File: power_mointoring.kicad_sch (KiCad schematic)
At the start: 30 parts, among them J10 Servo pwr, J11 Vin, J13 VCC, J14 +5V, J7 VCC, J8 Servo pwr, J9 BATT in, SW5 POWER, U3 3V3 REG, U4 DS2438Z+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

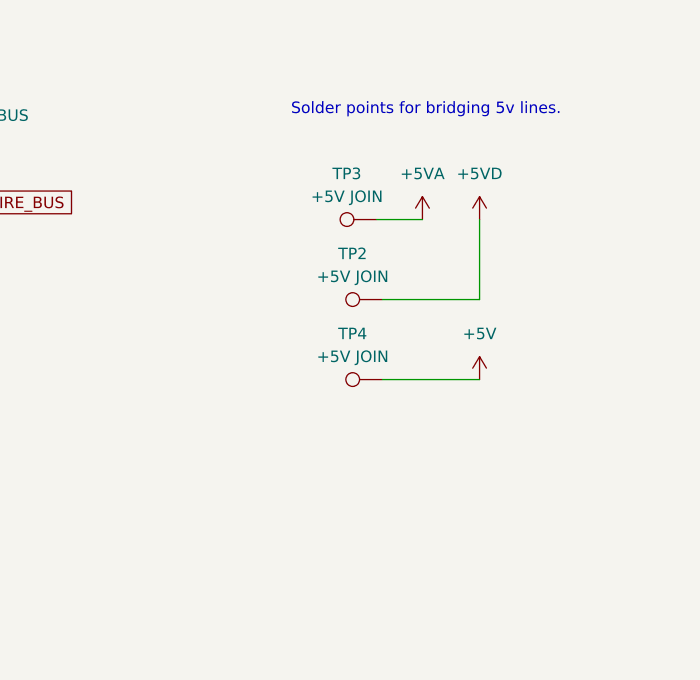
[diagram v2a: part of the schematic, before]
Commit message: Added missing power bridge point for 1 rail.
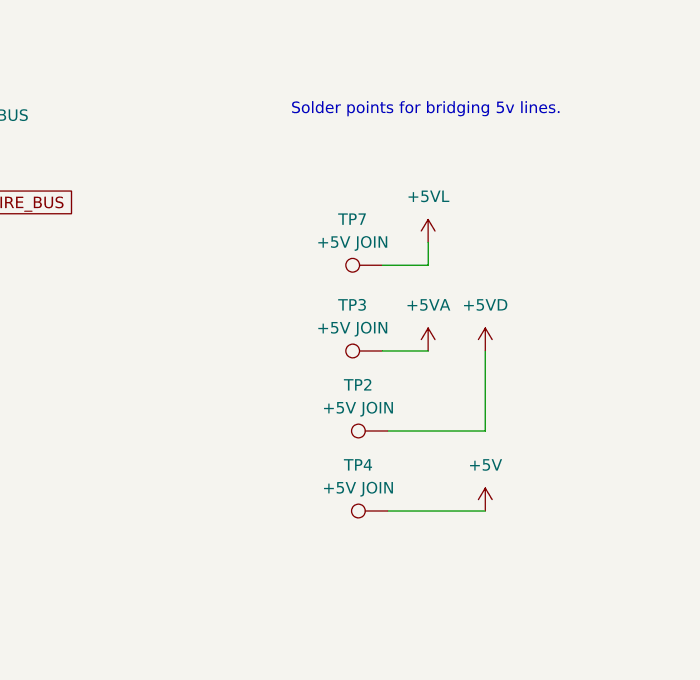
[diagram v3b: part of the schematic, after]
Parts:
- added TP7: +5V JOIN, TestPoint:TestPoint_Pad_D2.0mm, symbol Connector:TestPoint
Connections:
- net +5VL: now also TP7.1
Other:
- moved on the sheet: TP2, TP3, TP4
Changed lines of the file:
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@@
     (stroke (width 0) (type default))
   )
-  (wire (pts (xy 248.92 136.525) (xy 259.715 136.525))
+  (wire (pts (xy 249.555 151.13) (xy 260.35 151.13))
     (stroke (width 0) (type default))
   )
@@
     (stroke (width 0) (type default))
   )
-  (wire (pts (xy 248.92 127.635) (xy 259.715 127.635))
+  (wire (pts (xy 249.555 142.24) (xy 260.35 142.24))
     (stroke (width 0) (type default))
   )
@@
     (stroke (width 0) (type default))
   )
-  (wire (pts (xy 259.715 127.635) (xy 259.715 118.745))
-    (stroke (width 0) (type default))
-  )
-  (wire (pts (xy 248.285 118.745) (xy 253.365 118.745))
+  (wire (pts (xy 260.35 142.24) (xy 260.35 133.35))
+    (stroke (width 0) (type default))
+  )
+  (wire (pts (xy 248.92 133.35) (xy 254 133.35))
     (stroke (width 0) (type default))
   )
@@
     (stroke (width 0) (type default))
   )
+  (wire (pts (xy 254 121.285) (xy 254 123.825))
+    (stroke (width 0) (type default))
+  )
   (wire (pts (xy 133.35 152.4) (xy 147.32 152.4))
     (stroke (width 0) (type default))
@@
   )
   (wire (pts (xy 77.47 30.48) (xy 77.47 35.56))
+    (stroke (width 0) (type default))
+  )
+  (wire (pts (xy 248.92 123.825) (xy 254 123.825))
     (stroke (width 0) (type default))
   )
@@
     )
   )
-  (symbol (lib_id "Connector:TestPoint") (at 248.92 136.525 90) (unit 1)
-    (in_bom yes) (on_board yes) (dnp no) (fields_autoplaced)
-    (property "Reference" "TP4" (at 245.618 131.445 90)
-      (effects (font (size 1.27 1.27)))
-    )
-    (property "Value" "+5V JOIN" (at 245.618 133.985 90)
-      (effects (font (size 1.27 1.27)))
-    )
-    (property "Footprint" "TestPoint:TestPoint_Pad_D2.0mm" (at 248.92 131.445 0)
-      (effects (font (size 1.27 1.27)) hide)
-    )
-    (property "Datasheet" "~" (at 248.92 131.445 0)
+  (symbol (lib_id "Connector:TestPoint") (at 249.555 151.13 90) (unit 1)
+    (in_bom yes) (on_board yes) (dnp no) (fields_autoplaced)
+    (property "Reference" "TP4" (at 246.253 146.05 90)
+      (effects (font (size 1.27 1.27)))
+    )
+    (property "Value" "+5V JOIN" (at 246.253 148.59 90)
+      (effects (font (size 1.27 1.27)))
+    )
+    (property "Footprint" "TestPoint:TestPoint_Pad_D2.0mm" (at 249.555 146.05 0)
+      (effects (font (size 1.27 1.27)) hide)
+    )
+    (property "Datasheet" "~" (at 249.555 146.05 0)
       (effects (font (size 1.27 1.27)) hide)
     )
@@
         (path "/762e1435-54f1-40a1-a522-bcedd8174116/78a56bae-3afa-4383-914f-3e74817e0e83"
           (reference "J8") (unit 1)
+        )
+      )
+    )
+  )
+  (symbol (lib_id "power:+5VL") (at 254 121.285 0) (unit 1)
+    (in_bom yes) (on_board yes) (dnp no) (fields_autoplaced)
+    (property "Reference" "#PWR018" (at 254 125.095 0)
+      (effects (font (size 1.27 1.27)) hide)
+    )
+    (property "Value" "+5VL" (at 254 116.205 0)
+      (effects (font (size 1.27 1.27)))
+    )
+    (property "Footprint" "" (at 254 121.285 0)
+      (effects (font (size 1.27 1.27)) hide)
+    )
+    (property "Datasheet" "" (at 254 121.285 0)
+      (effects (font (size 1.27 1.27)) hide)
+    )
+    (pin "1")
+    (instances
+      (project "robot"
+        (path "/762e1435-54f1-40a1-a522-bcedd8174116/78a56bae-3afa-4383-914f-3e74817e0e83"
+          (reference "#PWR018") (unit 1)
         )
       )
@@
     )
   )
-  (symbol (lib_id "power:+5V") (at 259.715 136.525 0) (unit 1)
-    (in_bom yes) (on_board yes) (dnp no) (fields_autoplaced)
-    (property "Reference" "#PWR06" (at 259.715 140.335 0)
-      (effects (font (size 1.27 1.27)) hide)
-    )
-    (property "Value" "+5V" (at 259.715 131.445 0)
-      (effects (font (size 1.27 1.27)))
-    )
-    (property "Footprint" "" (at 259.715 136.525 0)
-      (effects (font (size 1.27 1.27)) hide)
-    )
-    (property "Datasheet" "" (at 259.715 136.525 0)
+  (symbol (lib_id "power:+5V") (at 260.35 151.13 0) (unit 1)
+    (in_bom yes) (on_board yes) (dnp no) (fields_autoplaced)
+    (property "Reference" "#PWR06" (at 260.35 154.94 0)
+      (effects (font (size 1.27 1.27)) hide)
+    )
+    (property "Value" "+5V" (at 260.35 146.05 0)
+      (effects (font (size 1.27 1.27)))
+    )
+    (property "Footprint" "" (at 260.35 151.13 0)
+      (effects (font (size 1.27 1.27)) hide)
+    )
+    (property "Datasheet" "" (at 260.35 151.13 0)
       (effects (font (size 1.27 1.27)) hide)
     )
@@
     )
   )
-  (symbol (lib_id "power:+5VA") (at 253.365 118.745 0) (unit 1)
-    (in_bom yes) (on_board yes) (dnp no) (fields_autoplaced)
-    (property "Reference" "#PWR015" (at 253.365 122.555 0)
-      (effects (font (size 1.27 1.27)) hide)
-    )
-    (property "Value" "+5VA" (at 253.365 113.665 0)
-      (effects (font (size 1.27 1.27)))
-    )
-    (property "Footprint" "" (at 253.365 118.745 0)
-      (effects (font (size 1.27 1.27)) hide)
-    )
-    (property "Datasheet" "" (at 253.365 118.745 0)
+  (symbol (lib_id "power:+5VA") (at 254 133.35 0) (unit 1)
+    (in_bom yes) (on_board yes) (dnp no) (fields_autoplaced)
+    (property "Reference" "#PWR015" (at 254 137.16 0)
+      (effects (font (size 1.27 1.27)) hide)
+    )
+    (property "Value" "+5VA" (at 254 128.27 0)
+      (effects (font (size 1.27 1.27)))
+    )
+    (property "Footprint" "" (at 254 133.35 0)
+      (effects (font (size 1.27 1.27)) hide)
+    )
+    (property "Datasheet" "" (at 254 133.35 0)
       (effects (font (size 1.27 1.27)) hide)
     )
@@
     )
   )
-  (symbol (lib_id "power:+5VD") (at 259.715 118.745 0) (unit 1)
-    (in_bom yes) (on_board yes) (dnp no) (fields_autoplaced)
-    (property "Reference" "#PWR016" (at 259.715 122.555 0)
-      (effects (font (size 1.27 1.27)) hide)
-    )
-    (property "Value" "+5VD" (at 259.715 113.665 0)
-      (effects (font (size 1.27 1.27)))
-    )
-    (property "Footprint" "" (at 259.715 118.745 0)
-      (effects (font (size 1.27 1.27)) hide)
-    )
-    (property "Datasheet" "" (at 259.715 118.745 0)
+  (symbol (lib_id "power:+5VD") (at 260.35 133.35 0) (unit 1)
+    (in_bom yes) (on_board yes) (dnp no) (fields_autoplaced)
+    (property "Reference" "#PWR016" (at 260.35 137.16 0)
+      (effects (font (size 1.27 1.27)) hide)
+    )
+    (property "Value" "+5VD" (at 260.35 128.27 0)
+      (effects (font (size 1.27 1.27)))
+    )
+    (property "Footprint" "" (at 260.35 133.35 0)
+      (effects (font (size 1.27 1.27)) hide)
+    )
+    (property "Datasheet" "" (at 260.35 133.35 0)
       (effects (font (size 1.27 1.27)) hide)
     )
@@
     )
   )
+  (symbol (lib_id "Connector:TestPoint") (at 248.92 123.825 90) (unit 1)
+    (in_bom yes) (on_board yes) (dnp no) (fields_autoplaced)
+    (property "Reference" "TP7" (at 245.618 118.745 90)
+      (effects (font (size 1.27 1.27)))
+    )
+    (property "Value" "+5V JOIN" (at 245.618 121.285 90)
+      (effects (font (size 1.27 1.27)))
+    )
+    (property "Footprint" "TestPoint:TestPoint_Pad_D2.0mm" (at 248.92 118.745 0)
+      (effects (font (size 1.27 1.27)) hide)
+    )
+    (property "Datasheet" "~" (at 248.92 118.745 0)
+      (effects (font (size 1.27 1.27)) hide)
+    )
+    (pin "1")
+    (instances
+      (project "robot"
+        (path "/762e1435-54f1-40a1-a522-bcedd8174116/78a56bae-3afa-4383-914f-3e74817e0e83"
+          (reference "TP7") (unit 1)
+        )
+      )
+    )
+  )
   (symbol (lib_id "power:GND") (at 97.79 191.77 0) (unit 1)
     (in_bom yes) (on_board yes) (dnp no) (fields_autoplaced)
@@
     )
   )
-  (symbol (lib_id "Connector:TestPoint") (at 248.92 127.635 90) (unit 1)
-    (in_bom yes) (on_board yes) (dnp no) (fields_autoplaced)
-    (property "Reference" "TP2" (at 245.618 122.555 90)
-      (effects (font (size 1.27 1.27)))
-    )
-    (property "Value" "+5V JOIN" (at 245.618 125.095 90)
-      (effects (font (size 1.27 1.27)))
-    )
-    (property "Footprint" "TestPoint:TestPoint_Pad_D2.0mm" (at 248.92 122.555 0)
-      (effects (font (size 1.27 1.27)) hide)
-    )
-    (property "Datasheet" "~" (at 248.92 122.555 0)
+  (symbol (lib_id "Connector:TestPoint") (at 249.555 142.24 90) (unit 1)
+    (in_bom yes) (on_board yes) (dnp no) (fields_autoplaced)
+    (property "Reference" "TP2" (at 246.253 137.16 90)
+      (effects (font (size 1.27 1.27)))
+    )
+    (property "Value" "+5V JOIN" (at 246.253 139.7 90)
+      (effects (font (size 1.27 1.27)))
+    )
+    (property "Footprint" "TestPoint:TestPoint_Pad_D2.0mm" (at 249.555 137.16 0)
+      (effects (font (size 1.27 1.27)) hide)
+    )
+    (property "Datasheet" "~" (at 249.555 137.16 0)
       (effects (font (size 1.27 1.27)) hide)
     )
@@
     )
   )
-  (symbol (lib_id "Connector:TestPoint") (at 248.285 118.745 90) (unit 1)
-    (in_bom yes) (on_board yes) (dnp no) (fields_autoplaced)
-    (property "Reference" "TP3" (at 244.983 113.665 90)
-      (effects (font (size 1.27 1.27)))
-    )
-    (property "Value" "+5V JOIN" (at 244.983 116.205 90)
-      (effects (font (size 1.27 1.27)))
-    )
-    (property "Footprint" "TestPoint:TestPoint_Pad_D2.0mm" (at 248.285 113.665 0)
-      (effects (font (size 1.27 1.27)) hide)
-    )
-    (property "Datasheet" "~" (at 248.285 113.665 0)
-      (effects (font (size 1.27 1.27)) hide)
-    )
+  (symbol (lib_id "Connector:TestPoint") (at 248.92 133.35 90) (unit 1)
+    (in_bom yes) (on_board yes) (dnp no) (fields_autoplaced)
+    (property "Reference" "TP3" (at 245.618 128.27 90)
+      (effects (font (size 1.27 1.27)))
+    )
+    (property "Value" "+5V JOIN" (at 245.618 130.81 90)
+      (effects (font (size 1.27 1.27)))
+    )
+    (property "Footprint" "TestPoint:TestPoint_Pad_D2.0mm" (at 248.92 128.27 0)
+      (effects (font (size 1.27 1.27)) hide)
+    )
+    (property "Datasheet" "~" (at 248.92 128.27 0)
+      (effects (font (size 1.27 1.27)) hide)
+    )

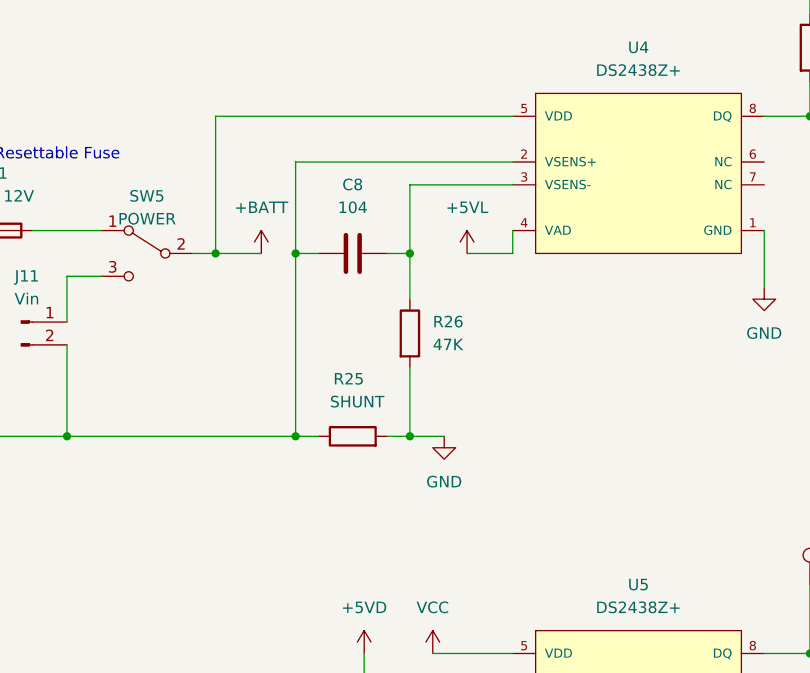
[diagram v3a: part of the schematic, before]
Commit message: Flipped current sense resistor connections - it was the wrong way around.
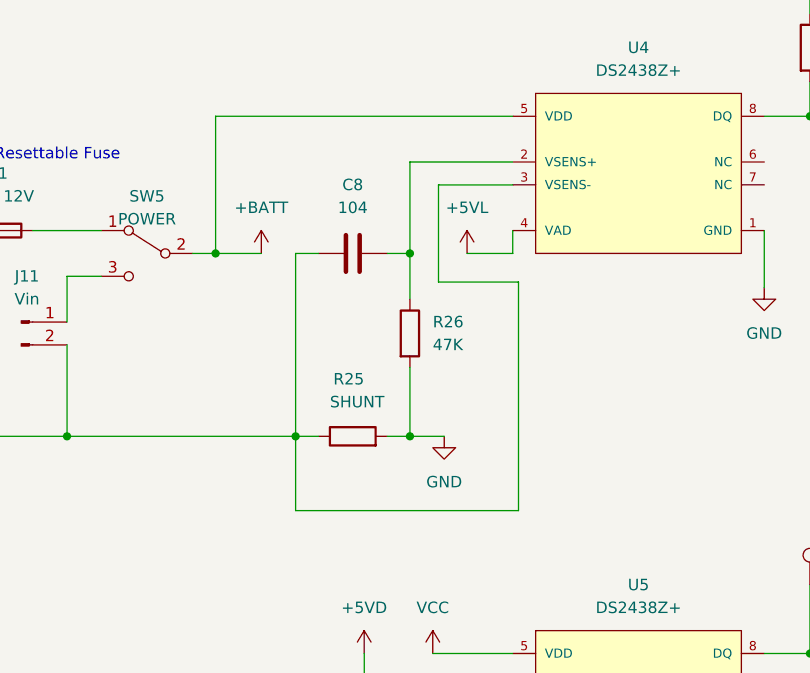
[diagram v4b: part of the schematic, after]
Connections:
- net at C8.2, J11.2 (Pin_2), J9.2 (Pin_2)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: now also U4.3 (VSENS-); no longer U4.2 (VSENS+)
- net at C8.1, R26.1: now also U4.2 (VSENS+); no longer U4.3 (VSENS-)
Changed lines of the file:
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@@
   (junction (at 77.47 43.18) (diameter 0) (color 0 0 0 0)
-  )
-  (junction (at 137.16 72.39) (diameter 0) (color 0 0 0 0)
   )
   (junction (at 149.86 92.71) (diameter 0) (color 0 0 0 0)
@@
     (stroke (width 0) (type default))
   )
+  (wire (pts (xy 161.925 100.965) (xy 137.16 100.965))
+    (stroke (width 0) (type default))
+  )
   (wire (pts (xy 149.86 92.71) (xy 153.67 92.71))
     (stroke (width 0) (type default))
@@
   )
   (wire (pts (xy 111.76 80.01) (xy 111.76 74.93))
+    (stroke (width 0) (type default))
+  )
+  (wire (pts (xy 161.29 64.77) (xy 153.035 64.77))
     (stroke (width 0) (type default))
   )
@@
     (stroke (width 0) (type default))
   )
+  (wire (pts (xy 137.16 100.965) (xy 137.16 92.71))
+    (stroke (width 0) (type default))
+  )
   (wire (pts (xy 57.15 35.56) (xy 44.45 35.56))
     (stroke (width 0) (type default))
@@
     (stroke (width 0) (type default))
   )
+  (wire (pts (xy 153.035 64.77) (xy 153.035 75.565))
+    (stroke (width 0) (type default))
+  )
   (wire (pts (xy 110.49 175.26) (xy 110.49 180.34))
     (stroke (width 0) (type default))
   )
-  (wire (pts (xy 137.16 62.23) (xy 161.29 62.23))
+  (wire (pts (xy 153.035 75.565) (xy 161.925 75.565))
     (stroke (width 0) (type default))
   )
@@
   )
   (wire (pts (xy 137.16 72.39) (xy 137.16 92.71))
+    (stroke (width 0) (type default))
+  )
+  (wire (pts (xy 149.86 62.23) (xy 161.29 62.23))
     (stroke (width 0) (type default))
   )
@@
     (stroke (width 0) (type default))
   )
-  (wire (pts (xy 137.16 62.23) (xy 137.16 72.39))
-    (stroke (width 0) (type default))
-  )
   (wire (pts (xy 64.77 43.18) (xy 64.77 46.99))
     (stroke (width 0) (type default))
@@
   )
   (wire (pts (xy 77.47 43.18) (xy 88.9 43.18))
+    (stroke (width 0) (type default))
+  )
+  (wire (pts (xy 161.925 75.565) (xy 161.925 100.965))
     (stroke (width 0) (type default))
   )
@@
     (stroke (width 0) (type default))
   )
-  (wire (pts (xy 161.29 64.77) (xy 149.86 64.77))
-    (stroke (width 0) (type default))
-  )
   (wire (pts (xy 97.79 92.71) (xy 111.76 92.71))
     (stroke (width 0) (type default))
   )
-  (wire (pts (xy 149.86 64.77) (xy 149.86 72.39))
+  (wire (pts (xy 149.86 62.23) (xy 149.86 72.39))
     (stroke (width 0) (type default))
   )
